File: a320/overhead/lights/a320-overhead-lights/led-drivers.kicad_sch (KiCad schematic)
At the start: 15 parts, among them J10 Conn_02x08_Odd_Even, J11 Conn_02x08_Odd_Even, J12 Conn_02x08_Odd_Even, J13 Conn_02x08_Odd_Even, J14 Conn_02x08_Odd_Even, J15 Conn_02x08_Odd_Even, U1 LED1642GWPTR, U2 LED1642GWPTR, U3 LED1642GWPTR

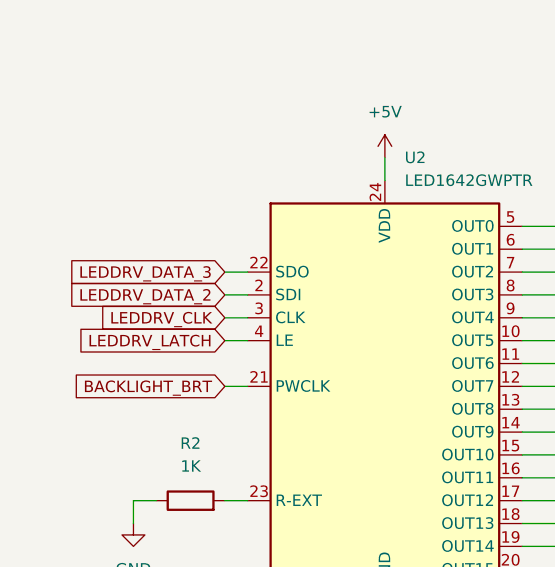
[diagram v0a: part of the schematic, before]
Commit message: a320 overhead lights - fixed wrong cascading of led drivers
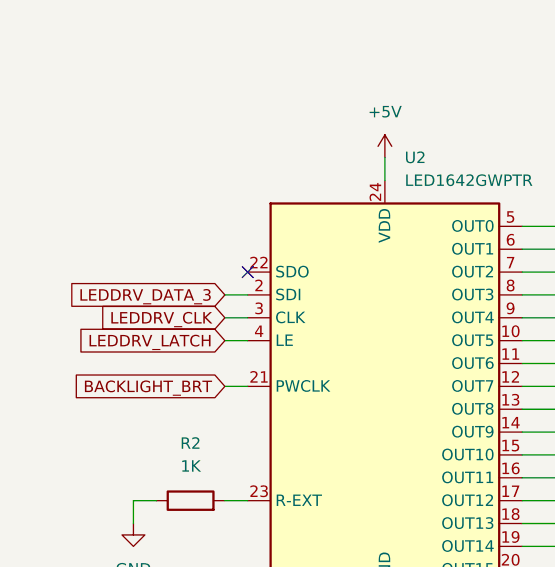
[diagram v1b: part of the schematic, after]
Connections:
- net LEDDRV_DATA_2: no longer U2.2 (SDI)
- net LEDDRV_DATA_3: now also U2.2 (SDI); no longer U2.22 (SDO)
- no-connect marks 0 -> 1
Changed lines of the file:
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@@
 		(color 0 0 0 0)
 	)
+	(no_connect
+		(at 48.26 134.62)
+	)
 	(wire
 		(pts
@@
 	(wire
 		(pts
-			(xy 45.72 134.62) (xy 48.26 134.62)
-		)
-		(stroke
-			(width 0)
-			(type default)
-		)
-	)
-	(wire
-		(pts
 			(xy 78.74 71.12) (xy 93.98 71.12)
 		)
@@
 		)
 	)
-	(global_label "LEDDRV_DATA_2"
+	(global_label "LEDDRV_DATA_3"
 		(shape input)
 		(at 45.72 137.16 180)
@@
 			(effects
 				(font
-					(size 1.27 1.27)
-				)
-				(justify right)
-				(hide yes)
-			)
-		)
-	)
-	(global_label "LEDDRV_DATA_3"
-		(shape input)
-		(at 45.72 134.62 180)
-		(fields_autoplaced yes)
-		(effects
-			(font
-				(size 1.27 1.27)
-			)
-			(justify right)
-		)
-		(property "Intersheetrefs" "${INTERSHEET_REFS}"
-			(at 28.0996 134.62 0)
-			(effects
-				(font
